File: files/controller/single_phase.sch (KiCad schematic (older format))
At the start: 12 parts, among them Q1 MOSFET-NCH-PSMN7R0, Q2 MOSFET-NCH-PSMN7R0, U1 MIC4604*

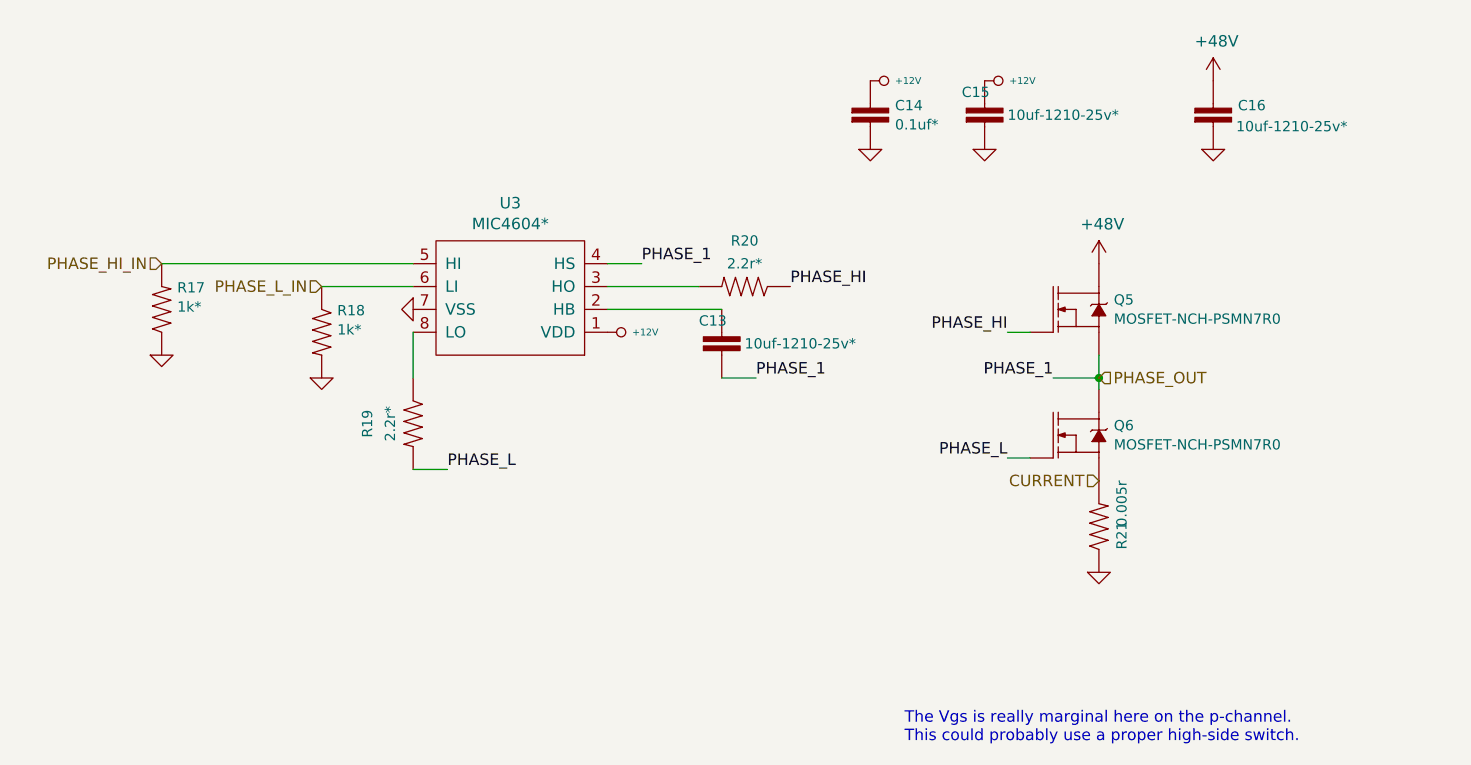
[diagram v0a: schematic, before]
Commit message: Changed component names
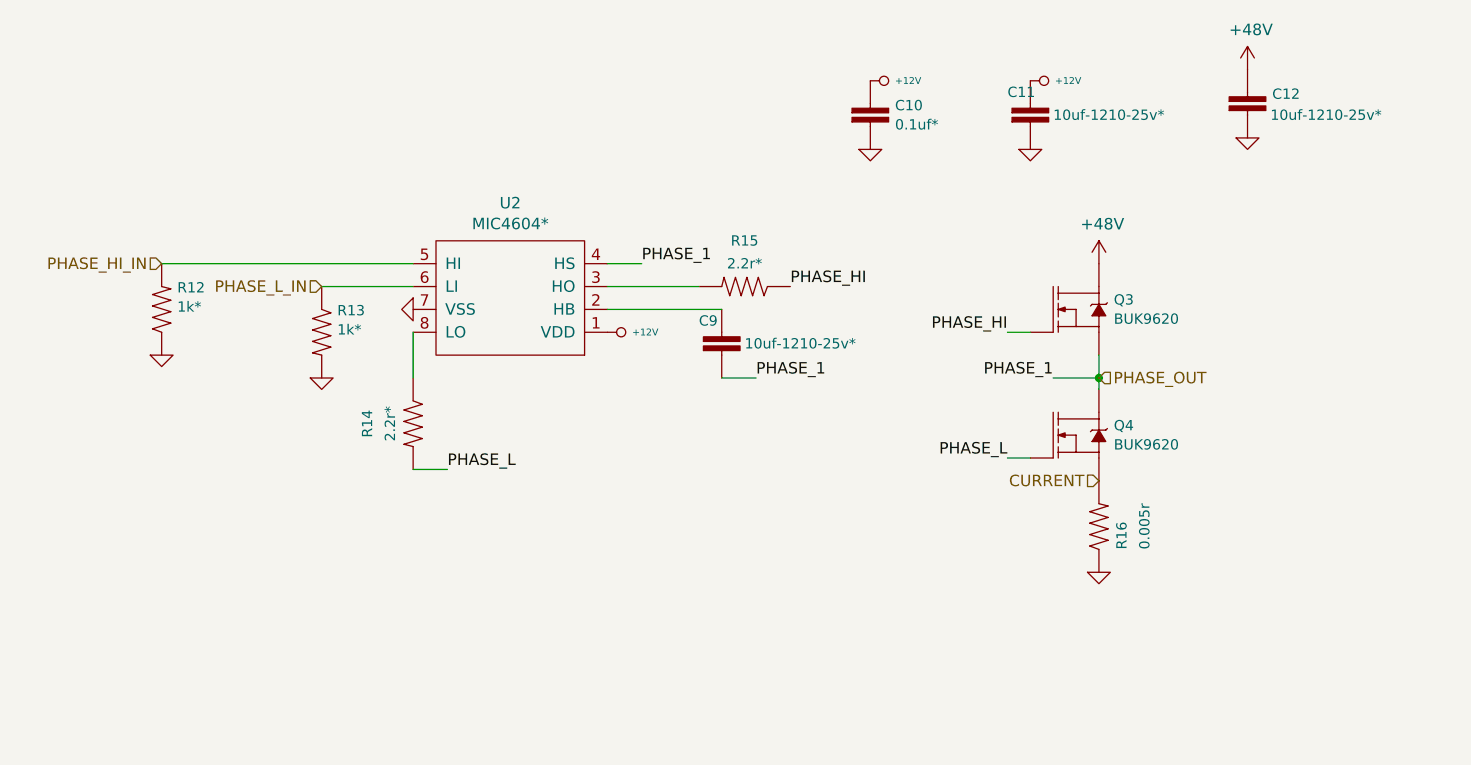
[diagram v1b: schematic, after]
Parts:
- Q1, Q2: value MOSFET-NCH-PSMN7R0 -> BUK9620
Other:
- note removed: "The Vgs is really marginal here on the p-channel. \nThis could probably use a proper high-side switch."
- moved on the sheet: C11, C12
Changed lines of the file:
@@
 EESchema Schematic File Version 4
-LIBS:controller-cache
-EELAYER 26 0
+EELAYER 30 0
 EELAYER END
 $Descr A4 11693 8268
 encoding utf-8
-Sheet 4 4
+Sheet 3 4
 Title ""
 Date ""
@@
 AR Path="/5BA85AFE/5B71FA51" Ref="R17"  Part="1"
 AR Path="/5BA85AC4/5B71FA51" Ref="R12"  Part="1"
-F 0 "R17" V 2095 1982 45  0000 R CNN
+F 0 "R12" V 2095 1982 45  0000 R CNN
 F 1 "1k*" V 2011 1982 45  0000 R CNN
 F 2 "0603" H 2000 2200 20  0001 C CNN
@@
 AR Path="/5BA85AFE/5B71FA52" Ref="R18"  Part="1"
 AR Path="/5BA85AC4/5B71FA52" Ref="R13"  Part="1"
-F 0 "R18" V 2605 2218 45  0000 L CNN
+F 0 "R13" V 2605 2218 45  0000 L CNN
 F 1 "1k*" V 2689 2218 45  0000 L CNN
 F 2 "0603" H 2700 2300 20  0001 C CNN
@@
 AR Path="/5BA85AFE/5B71FA53" Ref="#PWR041"  Part="1"
 AR Path="/5BA85AC4/5B71FA53" Ref="#PWR029"  Part="1"
-F 0 "#PWR041" H 2700 2350 30  0001 C CNN
+F 0 "#PWR029" H 2700 2350 30  0001 C CNN
 F 1 "GND" H 2700 2280 30  0001 C CNN
 F 2 "" H 2700 2350 50  0001 C CNN
@@
 AR Path="/5BA85AFE/5B71FA54" Ref="R20"  Part="1"
 AR Path="/5BA85AC4/5B71FA54" Ref="R15"  Part="1"
-F 0 "R20" H 4550 1750 45  0000 C CNN
+F 0 "R15" H 4550 1750 45  0000 C CNN
 F 1 "2.2r*" H 4550 1850 45  0000 C CNN
 F 2 "0805" H 4550 2100 20  0001 C CNN
@@
 AR Path="/5BA85AFE/5B71FA55" Ref="R19"  Part="1"
 AR Path="/5BA85AC4/5B71FA55" Ref="R14"  Part="1"
-F 0 "R19" H 3100 2350 45  0000 C CNN
+F 0 "R14" H 3100 2350 45  0000 C CNN
 F 1 "2.2r*" H 3100 2450 45  0000 C CNN
 F 2 "0805" H 3100 2700 20  0001 C CNN
@@
 AR Path="/5BA85AFE/5B71FA56" Ref="C14"  Part="1"
 AR Path="/5BA85AC4/5B71FA56" Ref="C10"  Part="1"
-F 0 "C14" H 5208 1342 45  0000 L CNN
+F 0 "C10" H 5208 1342 45  0000 L CNN
 F 1 "0.1uf*" H 5208 1258 45  0000 L CNN
 F 2 "0603" H 5100 1500 20  0001 C CNN
@@
 AR Path="/5BA85AFE/5B71FA57" Ref="#PWR045"  Part="1"
 AR Path="/5BA85AC4/5B71FA57" Ref="#PWR033"  Part="1"
-F 0 "#PWR045" H 5100 1350 30  0001 C CNN
+F 0 "#PWR033" H 5100 1350 30  0001 C CNN
 F 1 "GND" H 5100 1280 30  0001 C CNN
 F 2 "" H 5100 1350 50  0001 C CNN
@@
 	1    0    0    -1
 $EndComp
-Text Notes 5250 3950 0    50   ~ 0
-The Vgs is really marginal here on the p-channel. \nThis could probably use a proper high-side switch.
 $Comp
 L 0xDBFB7:MIC4604 U?
@@
 AR Path="/5BA85AFE/5B71FA58" Ref="U3"  Part="1"
 AR Path="/5BA85AC4/5B71FA58" Ref="U2"  Part="1"
-F 0 "U3" H 4275 1585 50  0000 C CNN
+F 0 "U2" H 4275 1585 50  0000 C CNN
 F 1 "MIC4604*" H 4275 1676 50  0000 C CNN
 F 2 "Package_SO:SOIC-8_3.9x4.9mm_P1.27mm" H 3900 1850 50  0001 C CNN
@@
 AR Path="/5BA85AFE/5B71FA59" Ref="C13"  Part="1"
 AR Path="/5BA85AC4/5B71FA59" Ref="C9"  Part="1"
-F 0 "C13" H 4350 2400 45  0000 L CNN
+F 0 "C9" H 4350 2400 45  0000 L CNN
 F 1 "10uf-1210-25v*" H 4550 2300 45  0000 L CNN
 F 2 "1210" H 4450 2500 20  0001 C CNN
@@
 AR Path="/5BA85AFE/5B71FA5A" Ref="#PWR042"  Part="1"
 AR Path="/5BA85AC4/5B71FA5A" Ref="#PWR030"  Part="1"
-F 0 "#PWR042" H 3100 2050 30  0001 C CNN
+F 0 "#PWR030" H 3100 2050 30  0001 C CNN
 F 1 "GND" H 3100 1980 30  0001 C CNN
 F 2 "" H 3100 2050 50  0001 C CNN
@@
 AR Path="/5BA85AFE/5B71FA5B" Ref="#PWR040"  Part="1"
 AR Path="/5BA85AC4/5B71FA5B" Ref="#PWR028"  Part="1"
-F 0 "#PWR040" H 2000 2250 30  0001 C CNN
+F 0 "#PWR028" H 2000 2250 30  0001 C CNN
 F 1 "GND" H 2000 2180 30  0001 C CNN
 F 2 "" H 2000 2250 50  0001 C CNN
@@
 L SparkFun-Capacitors:10UF-1210-50V-20% C?
 U 1 1 5B71FA5C
-P 5600 1250
+P 5800 1250
 AR Path="/5B71FA5C" Ref="C?"  Part="1"
 AR Path="/5B65AC1A/5B66E121/5B71FA5C" Ref="C?"  Part="1"
@@
 AR Path="/5BA85AFE/5B71FA5C" Ref="C15"  Part="1"
 AR Path="/5BA85AC4/5B71FA5C" Ref="C11"  Part="1"
-F 0 "C15" H 5500 1400 45  0000 L CNN
-F 1 "10uf-1210-25v*" H 5700 1300 45  0000 L CNN
-F 2 "1210" H 5600 1500 20  0001 C CNN
-F 3 "" H 5600 1250 50  0001 C CNN
-F 4 "1" H 5708 1216 60  0001 L CNN "arrange"
-	1    5600 1250
+F 0 "C11" H 5700 1400 45  0000 L CNN
+F 1 "10uf-1210-25v*" H 5900 1300 45  0000 L CNN
+F 2 "1210" H 5800 1500 20  0001 C CNN
+F 3 "" H 5800 1250 50  0001 C CNN
+F 4 "1" H 5908 1216 60  0001 L CNN "arrange"
+	1    5800 1250
 	1    0    0    -1
 $EndComp
@@
 L power:GND #PWR?
 U 1 1 5B71FA5D
-P 5600 1350
+P 5800 1350
 AR Path="/5B71FA5D" Ref="#PWR?"  Part="1"
 AR Path="/5B65AC1A/5B66E121/5B71FA5D" Ref="#PWR?"  Part="1"
@@
 AR Path="/5BA85AFE/5B71FA5D" Ref="#PWR047"  Part="1"
 AR Path="/5BA85AC4/5B71FA5D" Ref="#PWR035"  Part="1"
-F 0 "#PWR047" H 5600 1350 30  0001 C CNN
-F 1 "GND" H 5600 1280 30  0001 C CNN
-F 2 "" H 5600 1350 50  0001 C CNN
-F 3 "" H 5600 1350 50  0001 C CNN
-	1    5600 1350
+F 0 "#PWR035" H 5800 1350 30  0001 C CNN
+F 1 "GND" H 5800 1280 30  0001 C CNN
+F 2 "" H 5800 1350 50  0001 C CNN
+F 3 "" H 5800 1350 50  0001 C CNN
+	1    5800 1350
 	1    0    0    -1
 $EndComp
@@
 L SparkFun-Capacitors:10UF-1210-50V-20% C?
 U 1 1 5B71FA60
-P 6600 1250
+P 6750 1200
 AR Path="/5B71FA60" Ref="C?"  Part="1"
 AR Path="/5B65AC1A/5B66E121/5B71FA60" Ref="C?"  Part="1"
@@
 AR Path="/5BA85AFE/5B71FA60" Ref="C16"  Part="1"
 AR Path="/5BA85AC4/5B71FA60" Ref="C12"  Part="1"
-F 0 "C16" H 6708 1342 45  0000 L CNN
-F 1 "10uf-1210-25v*" H 6700 1250 45  0000 L CNN
-F 2 "1210" H 6600 1500 20  0001 C CNN
-F 3 "" H 6600 1250 50  0001 C CNN
-F 4 "" H 6708 1216 60  0000 L CNN "Field4"
-	1    6600 1250
+F 0 "C12" H 6858 1292 45  0000 L CNN
+F 1 "10uf-1210-25v*" H 6850 1200 45  0000 L CNN
+F 2 "1210" H 6750 1450 20  0001 C CNN
+F 3 "" H 6750 1200 50  0001 C CNN
+F 4 "" H 6858 1166 60  0000 L CNN "Field4"
+	1    6750 1200
 	1    0    0    -1
 $EndComp
@@
 L power:GND #PWR?
 U 1 1 5B6A677C
-P 6600 1350
+P 6750 1300
 AR Path="/5B6A677C" Ref="#PWR?"  Part="1"
 AR Path="/5B65AC1A/5B6A677C" Ref="#PWR?"  Part="1"
@@
 AR Path="/5BA85AFE/5B6A677C" Ref="#PWR051"  Part="1"
 AR Path="/5BA85AC4/5B6A677C" Ref="#PWR039"  Part="1"
-F 0 "#PWR051" H 6600 1350 30  0001 C CNN
-F 1 "GND" H 6600 1280 30  0001 C CNN
-F 2 "" H 6600 1350 50  0001 C CNN
-F 3 "" H 6600 1350 50  0001 C CNN
-	1    6600 1350
+F 0 "#PWR039" H 6750 1300 30  0001 C CNN
+F 1 "GND" H 6750 1230 30  0001 C CNN
+F 2 "" H 6750 1300 50  0001 C CNN
+F 3 "" H 6750 1300 50  0001 C CNN
+	1    6750 1300
 	1    0    0    -1
 $EndComp
@@
 AR Path="/5BA85AFE/5BA83F51" Ref="Q5"  Part="1"
 AR Path="/5BA85AC4/5BA83F51" Ref="Q3"  Part="1"
-F 0 "Q5" H 6165 2092 45  0000 L CNN
-F 1 "MOSFET-NCH-PSMN7R0" H 6165 2008 45  0000 L CNN
+F 0 "Q3" H 6165 2092 45  0000 L CNN
+F 1 "BUK9620" H 6165 2008 45  0000 L CNN
 F 2 "TO-263_D2PAK" H 6000 2300 20  0001 C CNN
 F 3 "" H 6000 2050 50  0001 C CNN
@@
 AR Path="/5BA85AFE/5BA88C34" Ref="#PWR043"  Part="1"
 AR Path="/5BA85AC4/5BA88C34" Ref="#PWR031"  Part="1"
-F 0 "#PWR043" H 3950 2100 20  0001 C CNN
+F 0 "#PWR031" H 3950 2100 20  0001 C CNN
 F 1 "+12V" V 3950 2258 30  0000 L CNN
 F 2 "" H 3950 2150 50  0001 C CNN
@@
 AR Path="/5BA83293/5BA8943D" Ref="#PWR024"  Part="1"
 AR Path="/5BA85AC4/5BA8943D" Ref="#PWR036"  Part="1"
-F 0 "#PWR048" H 6100 1700 50  0001 C CNN
+F 0 "#PWR036" H 6100 1700 50  0001 C CNN
 F 1 "+48V" H 6115 2023 50  0000 C CNN
 F 2 "" H 6100 1850 50  0001 C CNN
@@
 L power2:+48V #PWR?
 U 1 1 5BA89AA6
-P 6600 1050
+P 6750 1000
 AR Path="/5BA89AA6" Ref="#PWR?"  Part="1"
 AR Path="/5BA85AFE/5BA89AA6" Ref="#PWR050"  Part="1"
 AR Path="/5BA83293/5BA89AA6" Ref="#PWR026"  Part="1"
 AR Path="/5BA85AC4/5BA89AA6" Ref="#PWR038"  Part="1"
-F 0 "#PWR050" H 6600 900 50  0001 C CNN
-F 1 "+48V" H 6615 1223 50  0000 C CNN
-F 2 "" H 6600 1050 50  0001 C CNN
-F 3 "" H 6600 1050 50  0001 C CNN
-	1    6600 1050
+F 0 "#PWR038" H 6750 850 50  0001 C CNN
+F 1 "+48V" H 6765 1173 50  0000 C CNN
+F 2 "" H 6750 1000 50  0001 C CNN
+F 3 "" H 6750 1000 50  0001 C CNN
+	1    6750 1000
 	1    0    0    -1
 $EndComp
@@
 L power:+12V #PWR?
 U 1 1 5BA8A291
-P 5600 1050
+P 5800 1050
 AR Path="/5BA8A291" Ref="#PWR?"  Part="1"
 AR Path="/5BA83293/5BA8A291" Ref="#PWR022"  Part="1"
 AR Path="/5BA85AFE/5BA8A291" Ref="#PWR046"  Part="1"
 AR Path="/5BA85AC4/5BA8A291" Ref="#PWR034"  Part="1"
-F 0 "#PWR046" H 5600 1000 20  0001 C CNN
-F 1 "+12V" V 5600 1158 30  0000 L CNN
-F 2 "" H 5600 1050 50  0001 C CNN
-F 3 "" H 5600 1050 50  0001 C CNN
-	1    5600 1050
+F 0 "#PWR034" H 5800 1000 20  0001 C CNN
+F 1 "+12V" V 5800 1158 30  0000 L CNN
+F 2 "" H 5800 1050 50  0001 C CNN
+F 3 "" H 5800 1050 50  0001 C CNN
+	1    5800 1050
 	0    1    1    0
 $EndComp
@@
 AR Path="/5BA85AFE/5BA8A2BC" Ref="#PWR044"  Part="1"
 AR Path="/5BA85AC4/5BA8A2BC" Ref="#PWR032"  Part="1"
-F 0 "#PWR044" H 5100 1000 20  0001 C CNN
+F 0 "#PWR032" H 5100 1000 20  0001 C CNN
 F 1 "+12V" V 5100 1158 30  0000 L CNN
 F 2 "" H 5100 1050 50  0001 C CNN
@@
 AR Path="/5BA85AFE/5BA84288" Ref="Q6"  Part="1"
 AR Path="/5BA85AC4/5BA84288" Ref="Q4"  Part="1"
-F 0 "Q6" H 6165 2642 45  0000 L CNN
-F 1 "MOSFET-NCH-PSMN7R0" H 6165 2558 45  0000 L CNN
+F 0 "Q4" H 6165 2642 45  0000 L CNN
+F 1 "BUK9620" H 6165 2558 45  0000 L CNN
 F 2 "TO-263_D2PAK" H 6000 2850 20  0001 C CNN
 F 3 "" H 6000 2600 50  0001 C CNN
@@
 AR Path="/5BA85AFE/5BAFC399" Ref="R21"  Part="1"
 AR Path="/5BA85AC4/5BAFC399" Ref="R16"  Part="1"
-F 0 "R21" H 6000 2900 45  0000 L CNN
-F 1 "0.005r" H 6100 2900 45  0000 L CNN
+F 0 "R16" H 6000 2900 45  0000 L CNN
+F 1 "0.005r" H 6000 2800 45  0000 L CNN
 F 2 "1206" H 6100 3150 20  0001 C CNN
 F 3 "" H 6100 3000 60  0001 C CNN
@@
 AR Path="/5BA85AFE/5BAFC560" Ref="#PWR049"  Part="1"
 AR Path="/5BA85AC4/5BAFC560" Ref="#PWR037"  Part="1"
-F 0 "#PWR049" H 6100 3200 30  0001 C CNN
+F 0 "#PWR037" H 6100 3200 30  0001 C CNN
 F 1 "GND" H 6100 3130 30  0001 C CNN
 F 2 "" H 6100 3200 50  0001 C CNN
